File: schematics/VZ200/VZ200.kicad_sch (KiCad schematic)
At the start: 24 parts, among them J900 9V IN, SW900 PWR SW, U10 2364, U13 74LS04, U4 Z-80A, U9 2364, U900 LM7805, Y900 3.58MHz

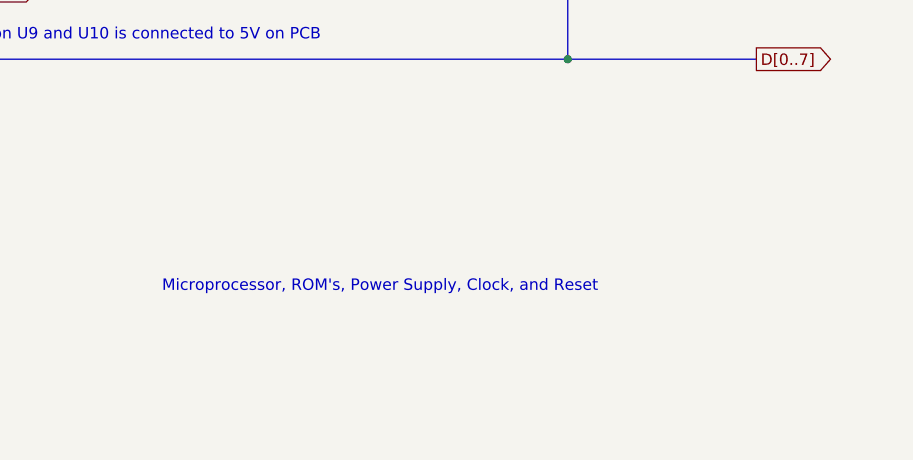
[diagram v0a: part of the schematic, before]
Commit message: Schematic for the VZ200 printer interface
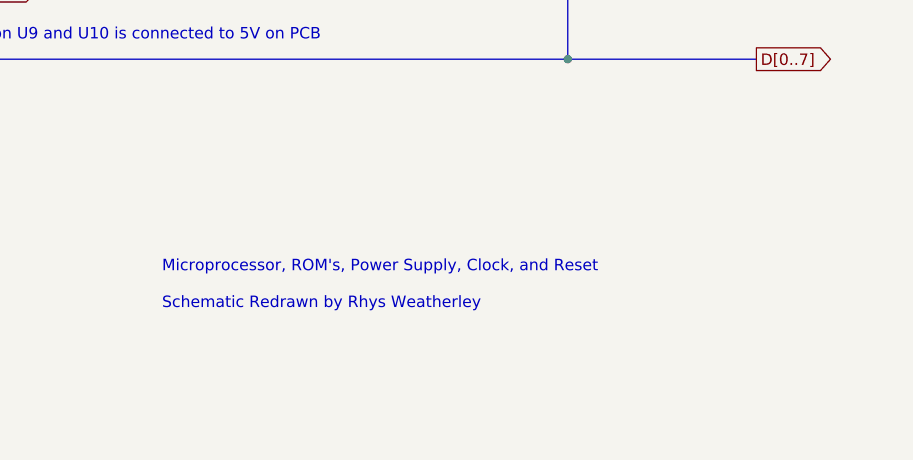
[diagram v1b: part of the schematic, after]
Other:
- note added: "Microprocessor, ROM's, Power Supply, Clock, and Reset Schematic Redrawn by Rhys Weatherley"
- note removed: "Microprocessor, ROM's, Power Supply, Clock, and Reset"
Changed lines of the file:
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@@
     (effects (font (size 1.27 1.27)) (justify left bottom))
   )
-  (text "Microprocessor, ROM's, Power Supply, Clock, and Reset"
-    (at 185.42 174.625 0)
+  (text "Microprocessor, ROM's, Power Supply, Clock, and Reset\n\nSchematic Redrawn by Rhys Weatherley"
+    (at 185.42 176.53 0)
     (effects (font (size 1.27 1.27)) (justify left bottom))
   )

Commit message: Add title and revision details to the schematic sheets
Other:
- title: (none) -> VZ200 Computer
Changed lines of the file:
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@@
 (kicad_sch (version 20230121) (generator eeschema)
   (paper "A4")
+  (title_block
+    (title "VZ200 Computer")
+    (date "2024-01-01")
+    (rev "1")
+  )
   (junction (at 137.795 148.59) (diameter 0) (color 0 0 0 0)
   )

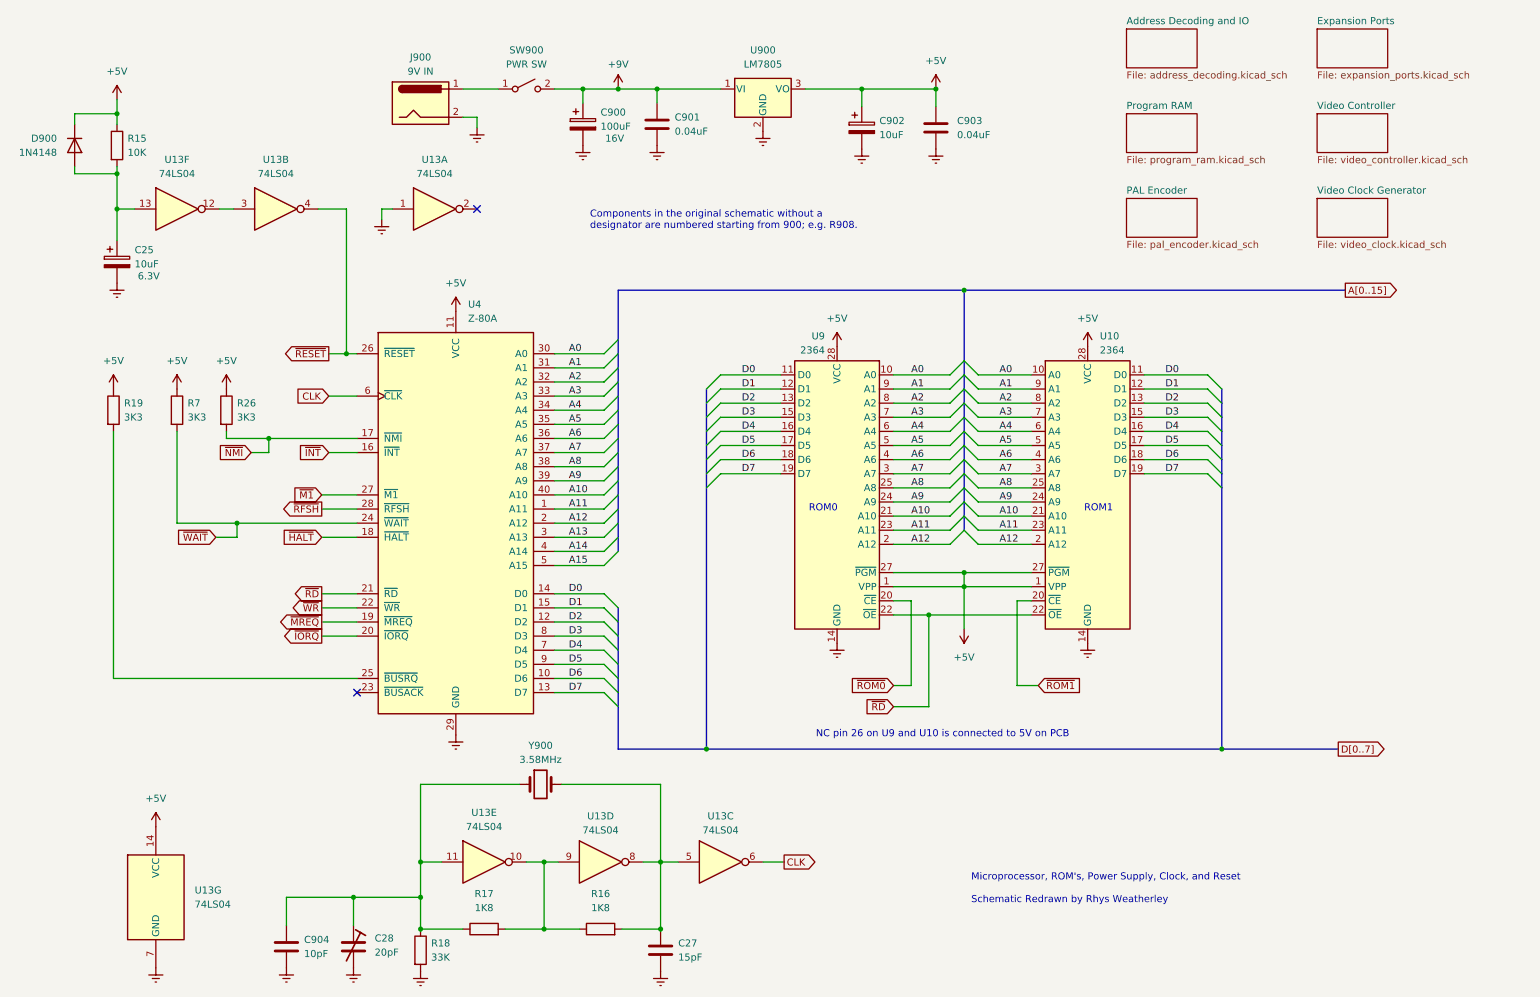
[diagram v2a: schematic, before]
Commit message: Update motherboard schematic based on inspection of the actual board
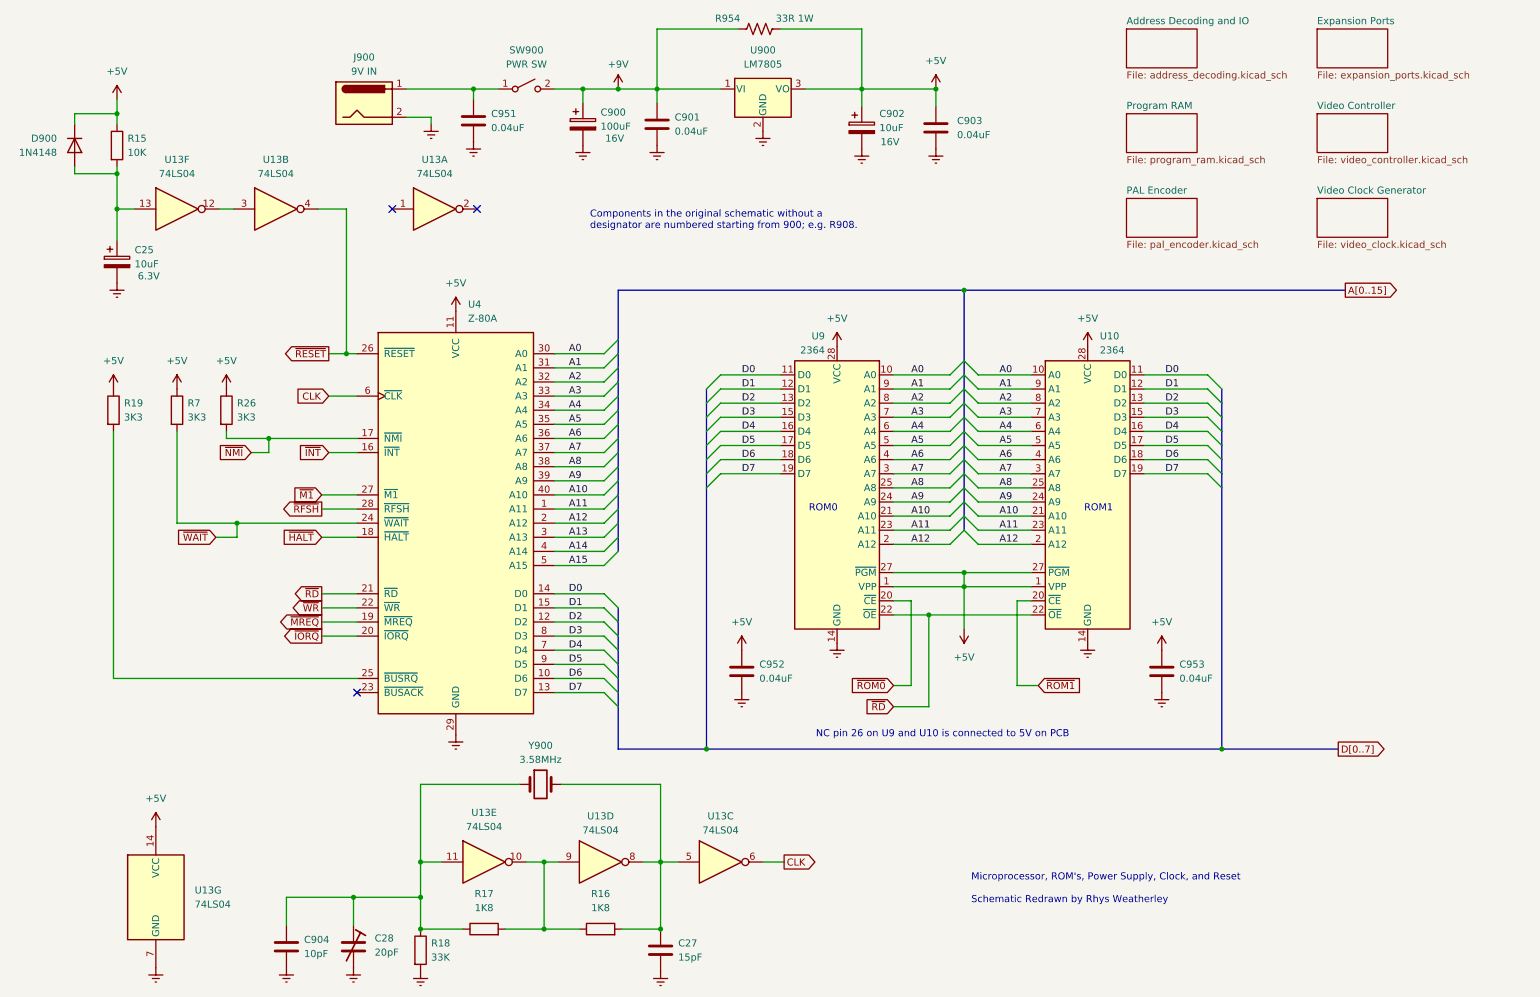
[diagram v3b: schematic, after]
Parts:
- added C951, C952, C953: 0.04uF, symbol Device:C
- added R954: 33R 1W, symbol Device:R_US
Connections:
- net +5V: now also C952.1, C953.1, R954.2
- net +9V: now also R954.1
- net Earth: now also C951.2, C952.2, C953.2; no longer U13.1
- net at J900.1, SW900.1 (A): now also C951.1
- no-connect marks 2 -> 3
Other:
- moved on the sheet: J900

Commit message: Restoration Part 2
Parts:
- U10, U9: value 2364 -> 2764
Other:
- note added: "2364 Pin 2764 Pin 1 / VPP 2 / A12 1 / A7 3 / A7 2 / A6 4 / A6 3 / A5 5 / A5 4 / A4 6 / A4 5 / A3 7 / A3 6 / A2 8 / A2 7 / A1 9 / A1 8 / A0 10 / A0 9 / D0 11 / D0 10 / D1 12 / D1 11 / D2 13 / D2 12 / GND 14 / GND"
- note added: "2364 Pin 2764 Pin 28 / VCC 27 / ~{PGM} 24 / VCC 26 / NC 23 / A8 25 / A8 22 / A9 24 / A9 21 / A12 23 / A11 20 / ~{CE} 22 / ~{OE} 19 / A10 21 / A10 18 / A11 20 / ~{CE} 17 / D7 19 / D7 16 / D6 18 / D6 15 / D5 17 / D5 14 / D4 16 / D4 13 / D3 15 / D3"
- note added: "The original schematic showed the ROM's as 28-pin, but the actual ROM's fitted to the PCB are 24-pin 2364's. The PCB has allowance for both 24-pin or 28-pin ROM's with bodge wires to remap things. The 28-pin 2764 or 28C64 can be used as replacements for the original ROM's with appropriate bodge wire adjustments."
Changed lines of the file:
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@@
+    (effects (font (size 1.27 1.27)) (justify left bottom))
+  )
+  (text "The original schematic showed the\nROM's as 28-pin, but the actual ROM's\nfitted to the PCB are 24-pin 2364's.\n\nThe PCB has allowance for both 24-pin\nor 28-pin ROM's with bodge wires to\nremap things.\n\nThe 28-pin 2764 or 28C64 can be used as\nreplacements for the original ROM's with\nappropriate bodge wire adjustments."
+    (at 235.585 99.06 0)
     (effects (font (size 1.27 1.27)) (justify left bottom))
   )
@@
     (effects (font (size 1.27 1.27)) (justify left bottom))
   )
+  (text "2364 Pin   2764 Pin\n\n             28 / VCC\n             27 / ~{PGM}\n24 / VCC    26 / NC\n23 / A8     25 / A8\n22 / A9     24 / A9\n21 / A12    23 / A11\n20 / ~{CE}     22 / ~{OE}\n19 / A10    21 / A10\n18 / A11    20 / ~{CE}\n17 / D7     19 / D7\n16 / D6     18 / D6\n15 / D5     17 / D5\n14 / D4     16 / D4\n13 / D3     15 / D3"
+    (at 258.445 131.445 0)
+    (effects (font (size 1 1)) (justify left bottom))
+  )
   (text "ROM0" (at 156.21 106.045 0)
     (effects (font (size 1.27 1.27)) (justify left bottom))
@@
   (text "NC pin 26 on U9 and U10 is connected to 5V on PCB" (at 157.48 146.685 0)
     (effects (font (size 1.27 1.27)) (justify left bottom))
+  )
+  (text "2364 Pin   2764 Pin\n\n             1 / VPP\n             2 / A12\n1 / A7      3 / A7\n2 / A6      4 / A6\n3 / A5      5 / A5\n4 / A4      6 / A4\n5 / A3      7 / A3\n6 / A2      8 / A2\n7 / A1      9 / A1\n8 / A0     10 / A0\n9 / D0     11 / D0\n10 / D1    12 / D1\n11 / D2    13 / D2\n12 / GND   14 / GND\n"
+    (at 235.585 131.445 0)
+    (effects (font (size 1 1)) (justify left bottom))
   )
   (label "A3" (at 113.03 85.09 0) (fields_autoplaced)
@@
   (symbol (lib_id "Memory_EPROM:2764") (at 206.375 101.6 0) (unit 1)
     (in_bom yes) (on_board yes) (dnp no) (fields_autoplaced)
-    (property "Reference" "U10" (at 208.5691 74.295 0)
-      (effects (font (size 1.27 1.27)) (justify left))
-    )
-    (property "Value" "2364" (at 208.5691 76.835 0)
+    (property "Reference" "U10" (at 208.5691 73.66 0)
+      (effects (font (size 1.27 1.27)) (justify left))
+    )
+    (property "Value" "2764" (at 208.5691 76.2 0)
       (effects (font (size 1.27 1.27)) (justify left))
     )
@@
       (effects (font (size 1.27 1.27)) (justify left))
     )
-    (property "Value" "2364" (at 159.0959 76.835 0)
-      (effects (font (size 1.27 1.27)) (justify left))
-    )
+    (property "Value" "2764" (at 159.0959 76.835 0)
+      (effects (font (size 1.27 1.27)) (justify left))
+    )
